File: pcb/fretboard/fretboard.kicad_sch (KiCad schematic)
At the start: 7 parts, among them J1 Conn_01x05_Pin

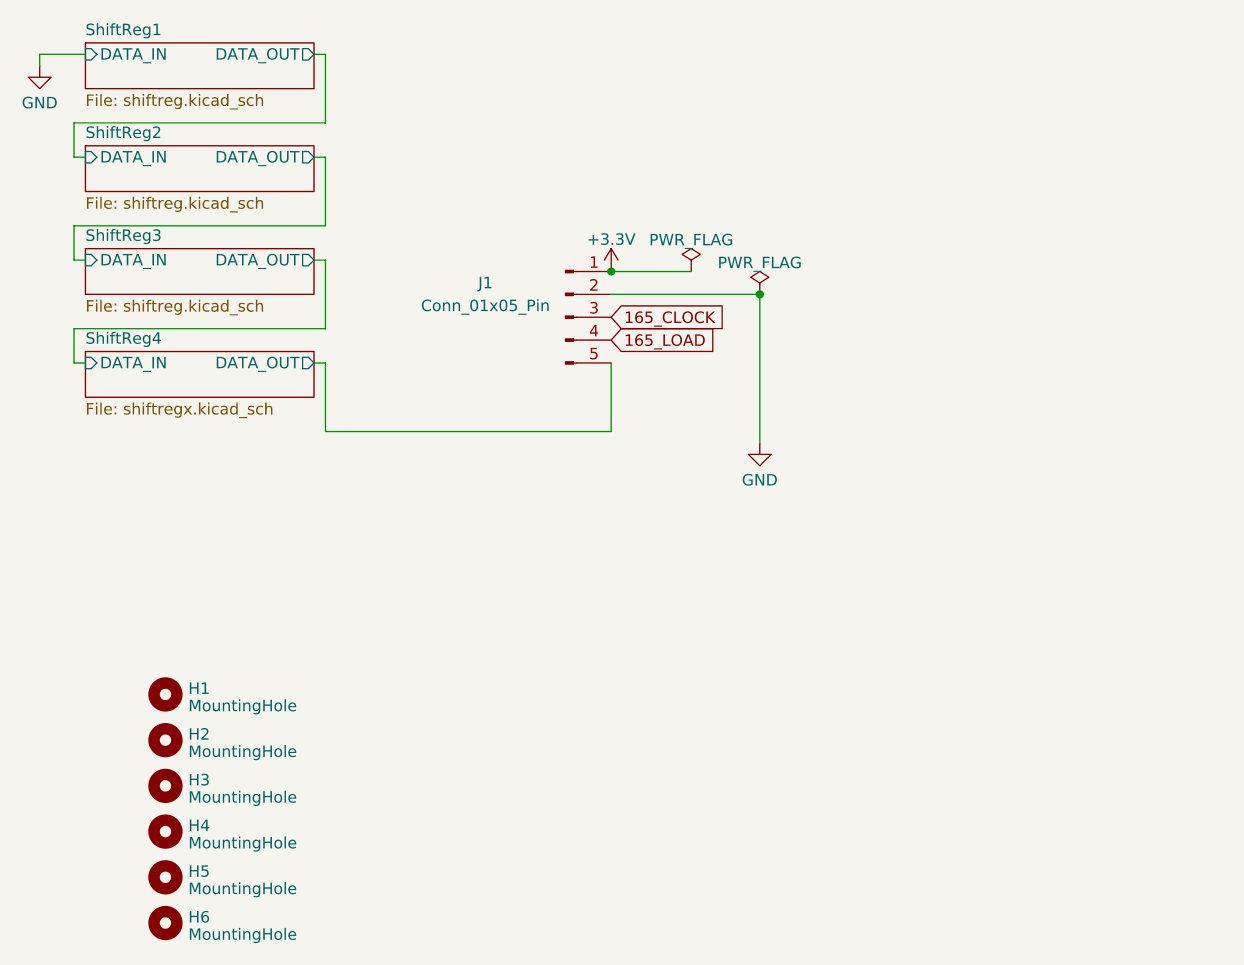
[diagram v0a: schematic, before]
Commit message: fretboard finished
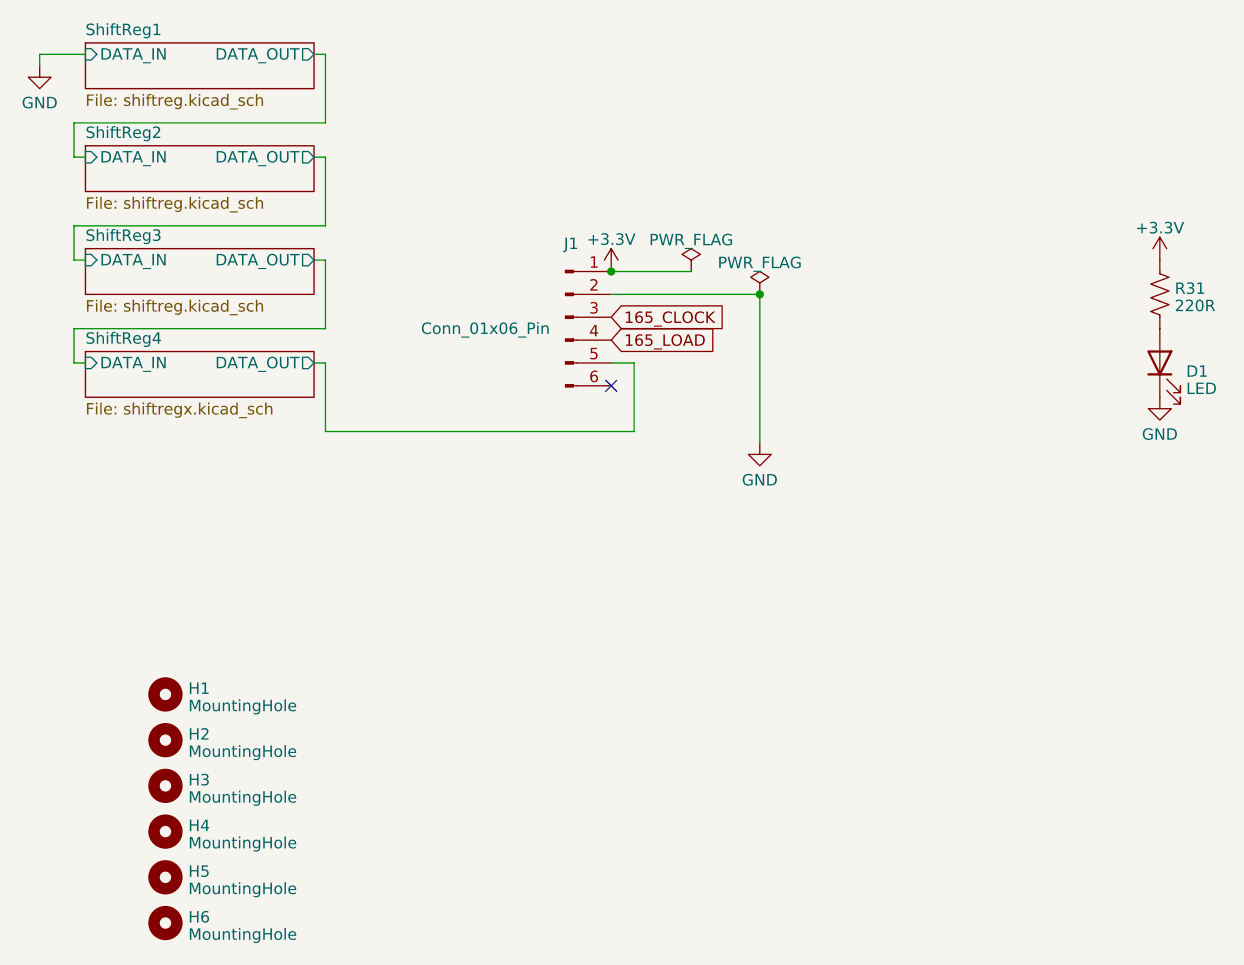
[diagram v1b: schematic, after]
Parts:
- removed J1: Conn_01x05_Pin, Bjarkar:bjarkar_fretboard_header, symbol Connector:Conn_01x05_Pin
- added D1: LED, LED_SMD:LED_0805_2012Metric, symbol Device:LED
- added J1: Conn_01x06_Pin, Bjarkar:jst zh fretboard connector, symbol Connector:Conn_01x06_Pin
- added R31: 220R, Resistor_SMD:R_0603_1608Metric, symbol Device:R_US
- H1, H2, H3, H4, H5, H6: footprint MountingHole:MountingHole_2.2mm_M2 -> Bjarkar:MountingHole_2.2mm_M2_countersunk
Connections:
- net +3.3V: now also J1.1 (Pin_1), R31.1
- net 165_CLOCK: now also J1.3 (Pin_3)
- net 165_LOAD: now also J1.4 (Pin_4)
- net GND: now also D1.1 (K), J1.2 (Pin_2)
- net ShiftReg4/DATA_OUT: now also J1.5 (Pin_5)
- new net: D1.2 (A), R31.2
- no-connect marks 0 -> 1
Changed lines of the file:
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@@
 (kicad_sch (version 20230121) (generator eeschema)
   (paper "A4")
+  (junction (at 182.88 85.09) (diameter 0) (color 0 0 0 0)
+  )
   (junction (at 166.37 82.55) (diameter 0) (color 0 0 0 0)
   )
-  (junction (at 182.88 85.09) (diameter 0) (color 0 0 0 0)
-  )
+  (no_connect (at 166.37 95.25))
   (wire (pts (xy 134.62 66.04) (xy 106.68 66.04))
     (stroke (width 0) (type default))
@@
     (stroke (width 0) (type default))
   )
-  (wire (pts (xy 134.62 100.33) (xy 166.37 100.33))
+  (wire (pts (xy 134.62 100.33) (xy 168.91 100.33))
+    (stroke (width 0) (type default))
+  )
+  (wire (pts (xy 168.91 92.71) (xy 166.37 92.71))
     (stroke (width 0) (type default))
   )
@@
     (stroke (width 0) (type default))
   )
-  (wire (pts (xy 166.37 100.33) (xy 166.37 92.71))
+  (wire (pts (xy 168.91 100.33) (xy 168.91 92.71))
     (stroke (width 0) (type default))
   )
@@
       (effects (font (size 1.27 1.27)) (justify left))
     )
-    (property "Footprint" "MountingHole:MountingHole_2.2mm_M2" (at 116.84 154.94 0)
+    (property "Footprint" "Bjarkar:MountingHole_2.2mm_M2_countersunk" (at 116.84 154.94 0)
       (effects (font (size 1.27 1.27)) hide)
     )
@@
     )
   )
+  (symbol (lib_id "Device:R_US") (at 227.33 85.09 0) (unit 1)
+    (in_bom yes) (on_board yes) (dnp no) (fields_autoplaced)
+    (property "Reference" "R31" (at 228.981 84.4463 0)
+      (effects (font (size 1.27 1.27)) (justify left))
+    )
+    (property "Value" "220R" (at 228.981 86.3673 0)
+      (effects (font (size 1.27 1.27)) (justify left))
+    )
+    (property "Footprint" "Resistor_SMD:R_0603_1608Metric" (at 228.346 85.344 90)
+      (effects (font (size 1.27 1.27)) hide)
+    )
+    (property "Datasheet" "~" (at 227.33 85.09 0)
+      (effects (font (size 1.27 1.27)) hide)
+    )
+    (pin "1")
+    (pin "2")
+    (instances
+      (project "fretboard"
+        (path "/b41ca7b2-6ea9-46e5-9fbc-53905fc7e403"
+          (reference "R31") (unit 1)
+        )
+      )
+    )
+  )
+  (symbol (lib_id "Device:LED") (at 227.33 92.71 90) (unit 1)
+    (in_bom yes) (on_board yes) (dnp no) (fields_autoplaced)
+    (property "Reference" "D1" (at 230.251 93.6538 90)
+      (effects (font (size 1.27 1.27)) (justify right))
+    )
+    (property "Value" "LED" (at 230.251 95.5748 90)
+      (effects (font (size 1.27 1.27)) (justify right))
+    )
+    (property "Footprint" "LED_SMD:LED_0805_2012Metric" (at 227.33 92.71 0)
+      (effects (font (size 1.27 1.27)) hide)
+    )
+    (property "Datasheet" "~" (at 227.33 92.71 0)
+      (effects (font (size 1.27 1.27)) hide)
+    )
+    (pin "1")
+    (pin "2")
+    (instances
+      (project "fretboard"
+        (path "/b41ca7b2-6ea9-46e5-9fbc-53905fc7e403"
+          (reference "D1") (unit 1)
+        )
+      )
+    )
+  )
+  (symbol (lib_id "power:+3.3V") (at 227.33 81.28 0) (unit 1)
+    (in_bom yes) (on_board yes) (dnp no) (fields_autoplaced)
+    (property "Reference" "#PWR?" (at 227.33 85.09 0)
+      (effects (font (size 1.27 1.27)) hide)
+    )
+    (property "Value" "+3.3V" (at 227.33 77.724 0)
+      (effects (font (size 1.27 1.27)))
+    )
+    (property "Footprint" "" (at 227.33 81.28 0)
+      (effects (font (size 1.27 1.27)) hide)
+    )
+    (property "Datasheet" "" (at 227.33 81.28 0)
+      (effects (font (size 1.27 1.27)) hide)
+    )
+    (pin "1")
+    (instances
+      (project "dk2_03_top"
+        (path "/87a59a99-d509-467e-85da-26d34072acb7"
+          (reference "#PWR?") (unit 1)
+        )
+        (path "/87a59a99-d509-467e-85da-26d34072acb7/c399aef9-3678-4747-9295-3eabdcc57d0c"
+          (reference "#PWR035") (unit 1)
+        )
+        (path "/87a59a99-d509-467e-85da-26d34072acb7/6f97e18f-9a2c-4988-a61c-f43e42f27b8b"
+          (reference "#PWR039") (unit 1)
+        )
+        (path "/87a59a99-d509-467e-85da-26d34072acb7/1a91e583-926b-4126-a95f-efd256f8eb1b"
+          (reference "#PWR011") (unit 1)
+        )
+      )
+      (project "fretboard"
+        (path "/b41ca7b2-6ea9-46e5-9fbc-53905fc7e403/21fb0463-5c17-4335-aab5-f07947500c5f"
+          (reference "#PWR01") (unit 1)
+        )
+        (path "/b41ca7b2-6ea9-46e5-9fbc-53905fc7e403/a4b9cdfb-80fd-4ef8-bf54-bd052ef6f1f6"
+          (reference "#PWR03") (unit 1)
+        )
+        (path "/b41ca7b2-6ea9-46e5-9fbc-53905fc7e403/5b36a1cd-dd8f-4ab7-9ce4-0c9849c29424"
+          (reference "#PWR05") (unit 1)
+        )
+        (path "/b41ca7b2-6ea9-46e5-9fbc-53905fc7e403/a8b72c19-8ea9-4c92-9888-a5af7cbf8516"
+          (reference "#PWR07") (unit 1)
+        )
+        (path "/b41ca7b2-6ea9-46e5-9fbc-53905fc7e403"
+          (reference "#PWR012") (unit 1)
+        )
+      )
+    )
+  )
   (symbol (lib_id "Mechanical:MountingHole") (at 116.84 139.7 0) (unit 1)
     (in_bom yes) (on_board yes) (dnp no) (fields_autoplaced)
@@
       (effects (font (size 1.27 1.27)) (justify left))
     )
-    (property "Footprint" "MountingHole:MountingHole_2.2mm_M2" (at 116.84 139.7 0)
+    (property "Footprint" "Bjarkar:MountingHole_2.2mm_M2_countersunk" (at 116.84 139.7 0)
       (effects (font (size 1.27 1.27)) hide)
     )
@@
     )
   )
-  (symbol (lib_id "Connector:Conn_01x05_Pin") (at 161.29 87.63 0) (unit 1)
+  (symbol (lib_id "Connector:Conn_01x06_Pin") (at 161.29 87.63 0) (unit 1)
     (in_bom yes) (on_board yes) (dnp no)
-    (property "Reference" "J1" (at 152.4 83.82 0)
-      (effects (font (size 1.27 1.27)))
-    )
-    (property "Value" "Conn_01x05_Pin" (at 152.4 86.36 0)
-      (effects (font (size 1.27 1.27)))
-    )
-    (property "Footprint" "Bjarkar:bjarkar_fretboard_header" (at 161.29 87.63 0)
+    (property "Reference" "J1" (at 161.925 79.4639 0)
+      (effects (font (size 1.27 1.27)))
+    )
+    (property "Value" "Conn_01x06_Pin" (at 152.4 88.9 0)
+      (effects (font (size 1.27 1.27)))
+    )
+    (property "Footprint" "Bjarkar:jst zh fretboard connector" (at 161.29 87.63 0)
       (effects (font (size 1.27 1.27)) hide)
     )
@@
     (pin "4")
     (pin "5")
+    (pin "6")
     (instances
       (project "fretboard"
@@
       (effects (font (size 1.27 1.27)) (justify left))
     )
-    (property "Footprint" "MountingHole:MountingHole_2.2mm_M2" (at 116.84 134.62 0)
+    (property "Footprint" "Bjarkar:MountingHole_2.2mm_M2_countersunk" (at 116.84 134.62 0)
       (effects (font (size 1.27 1.27)) hide)
     )
@@
       (effects (font (size 1.27 1.27)) (justify left))
     )
-    (property "Footprint" "MountingHole:MountingHole_2.2mm_M2" (at 116.84 129.54 0)
+    (property "Footprint" "Bjarkar:MountingHole_2.2mm_M2_countersunk" (at 116.84 129.54 0)
       (effects (font (size 1.27 1.27)) hide)
     )
@@
     )
   )
+  (symbol (lib_id "power:GND") (at 227.33 96.52 0) (unit 1)
+    (in_bom yes) (on_board yes) (dnp no) (fields_autoplaced)
+    (property "Reference" "#PWR036" (at 227.33 102.87 0)
+      (effects (font (size 1.27 1.27)) hide)
+    )
+    (property "Value" "GND" (at 227.33 100.6555 0)
+      (effects (font (size 1.27 1.27)))
+    )
+    (property "Footprint" "" (at 227.33 96.52 0)
+      (effects (font (size 1.27 1.27)) hide)
+    )
+    (property "Datasheet" "" (at 227.33 96.52 0)
+      (effects (font (size 1.27 1.27)) hide)
+    )
+    (pin "1")
+    (instances
+      (project "dk2_03_top"
+        (path "/87a59a99-d509-467e-85da-26d34072acb7/c399aef9-3678-4747-9295-3eabdcc57d0c"
+          (reference "#PWR036") (unit 1)
+        )
+        (path "/87a59a99-d509-467e-85da-26d34072acb7/6f97e18f-9a2c-4988-a61c-f43e42f27b8b"
+          (reference "#PWR040") (unit 1)
+        )
+        (path "/87a59a99-d509-467e-85da-26d34072acb7/1a91e583-926b-4126-a95f-efd256f8eb1b"
+          (reference "#PWR020") (unit 1)
+        )
+      )
+      (project "fretboard"
+        (path "/b41ca7b2-6ea9-46e5-9fbc-53905fc7e403/21fb0463-5c17-4335-aab5-f07947500c5f"
+          (reference "#PWR02") (unit 1)
+        )
+        (path "/b41ca7b2-6ea9-46e5-9fbc-53905fc7e403/a4b9cdfb-80fd-4ef8-bf54-bd052ef6f1f6"
+          (reference "#PWR04") (unit 1)
+        )
+        (path "/b41ca7b2-6ea9-46e5-9fbc-53905fc7e403/5b36a1cd-dd8f-4ab7-9ce4-0c9849c29424"
+          (reference "#PWR06") (unit 1)
+        )
+        (path "/b41ca7b2-6ea9-46e5-9fbc-53905fc7e403/a8b72c19-8ea9-4c92-9888-a5af7cbf8516"
+          (reference "#PWR08") (unit 1)
+        )
+        (path "/b41ca7b2-6ea9-46e5-9fbc-53905fc7e403"
+          (reference "#PWR013") (unit 1)
+        )
+      )
+    )
+  )
   (symbol (lib_id "Mechanical:MountingHole") (at 116.84 149.86 0) (unit 1)
     (in_bom yes) (on_board yes) (dnp no) (fields_autoplaced)
@@
       (effects (font (size 1.27 1.27)) (justify left))
     )
-    (property "Footprint" "MountingHole:MountingHole_2.2mm_M2" (at 116.84 149.86 0)
+    (property "Footprint" "Bjarkar:MountingHole_2.2mm_M2_countersunk" (at 116.84 149.86 0)
       (effects (font (size 1.27 1.27)) hide)
     )
@@
       (effects (font (size 1.27 1.27)) (justify left))
     )
-    (property "Footprint" "MountingHole:MountingHole_2.2mm_M2" (at 116.84 144.78 0)
-      (effects (font (size 1.27 1.27)) hide)
-    )
+    (property "Footprint" "Bjarkar:MountingHole_2.2mm_M2_countersunk" (at 116.84 144.78 0)
+      (effects (font (size 1.27 1.27)) hide)
+    )
